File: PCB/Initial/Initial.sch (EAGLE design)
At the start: 19 parts, among them U2 AT24C512C-SHD-B

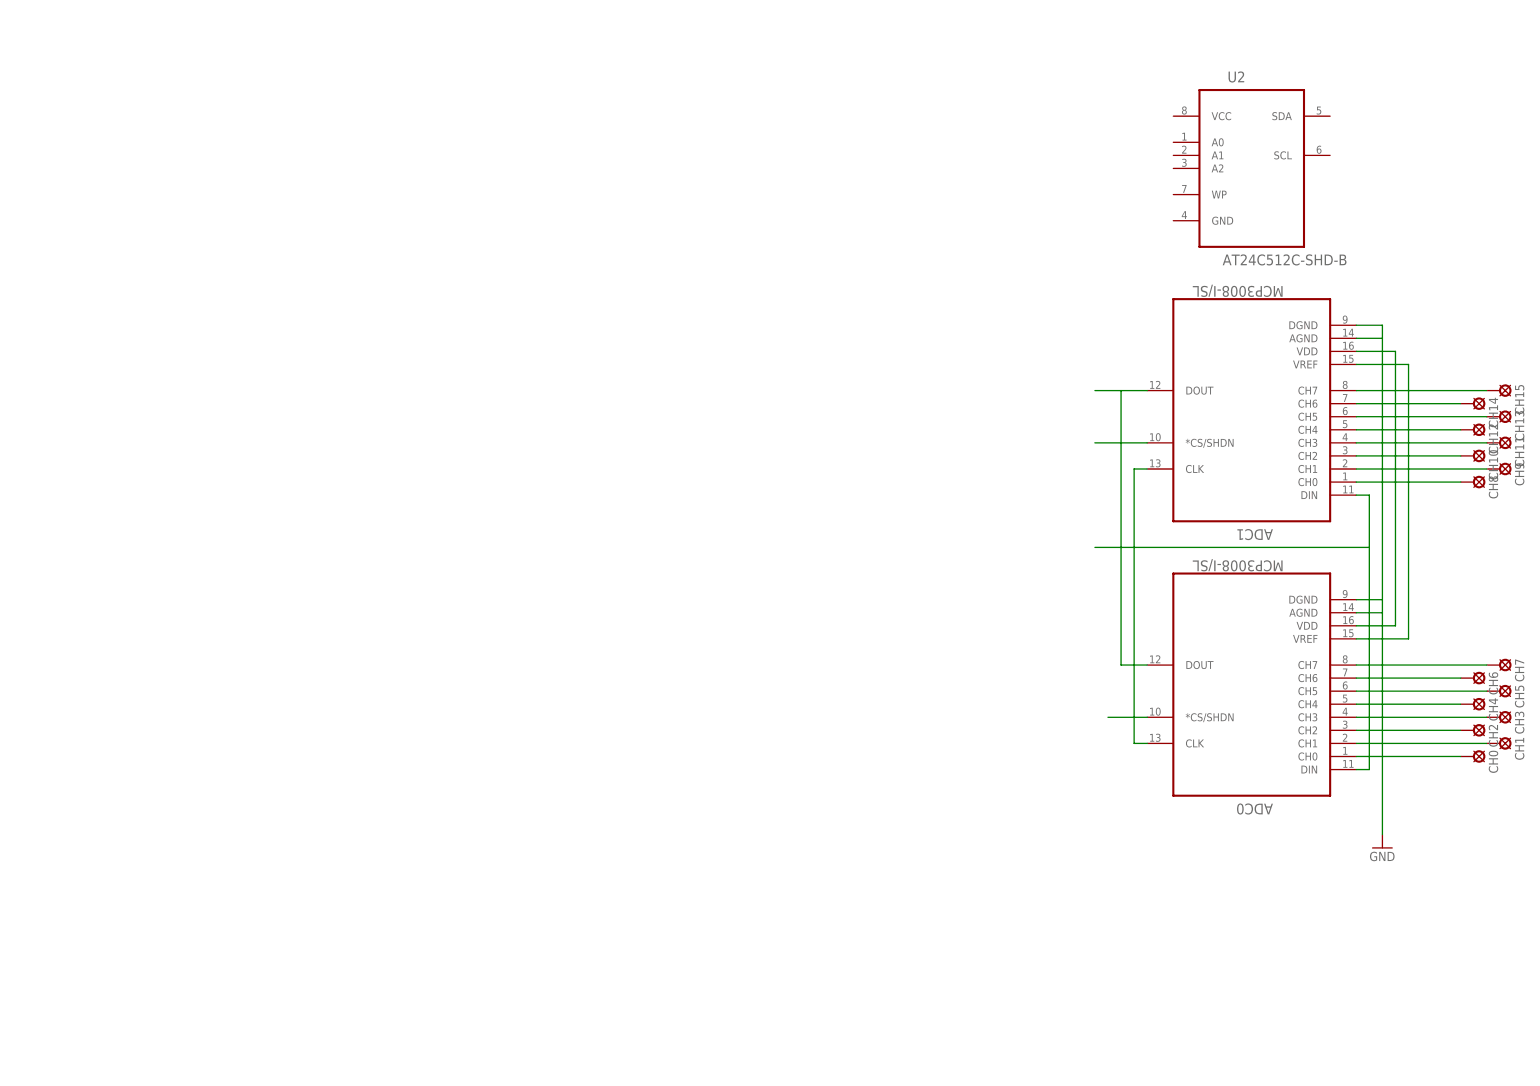
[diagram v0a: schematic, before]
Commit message: Need to draw Xtals, SPI_mini_interface, and probably some more. Might update center of CSR1010A05 with a ground pad. Need to double check SPI compatibility (might be overlayed with I2C)
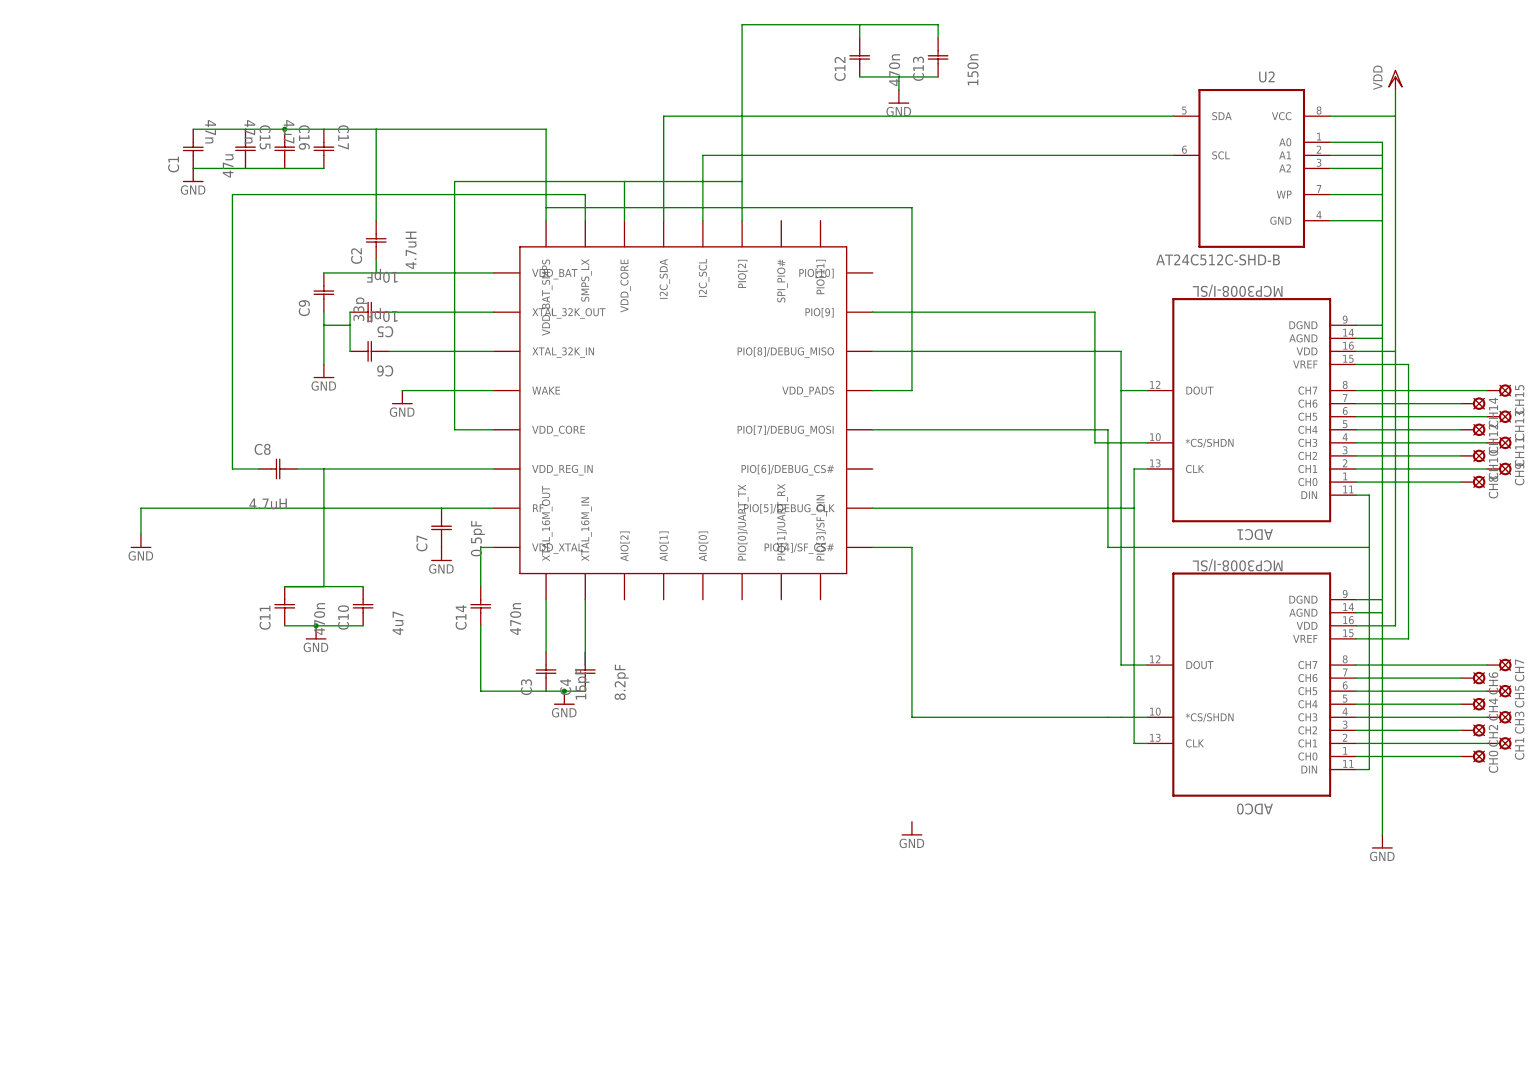
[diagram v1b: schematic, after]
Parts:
- added C1: 47u, AVX_By_element14_Batch_1:UQCL2A100JAT2A/500
- added C10: 4u7, AVX_By_element14_Batch_1:UQCL2A100JAT2A/500
- added C11, C12, C14: 470n, AVX_By_element14_Batch_1:UQCL2A100JAT2A/500
- added C13: 150n, AVX_By_element14_Batch_1:UQCL2A100JAT2A/500
- added C15, C16: 47n, AVX_By_element14_Batch_1:UQCL2A1R0BAT2A/500
- added C17: 4u7, AVX_By_element14_Batch_1:UQCL2A1R0BAT2A/500
- added C2: 4.7uH, AVX_By_element14_Batch_1:UQCL2A100JAT2A/500
- added C3: 15pF, AVX_By_element14_Batch_1:UQCL2A150JAT2A/500
- added C4: 8.2pF, AVX_By_element14_Batch_1:UQCL2A8R2CAT2A/500
- added C5, C6: 10pF, AVX_By_element14_Batch_1:UQCL2A100JAT2A/500
- added C7: 0.5pF, AVX_By_element14_Batch_1:UQCL2A0R5BAT2A/500
- added C8: 4.7uH, AVX_By_element14_Batch_1:1210AC103KAZ1A
- added C9: 33p, AVX_By_element14_Batch_1:UQCL2A100JAT2A/500
- added U$1: CSR1010A05-IQQM-R, CSR1010A05:CSR1010A05-IQQM-R
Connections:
- new net N$17: U$1.I2C_SDA, U2.SDA
- new net N$18: U$1.I2C_SCL, U2.SCL
- new net N$26: C6.C1, U$1.XTAL_32K_IN
- new net N$27: C5.C1, U$1.XTAL_32K_OUT
- new net N$28: C12.C2, C13.C2, U$1.PIO[2], U$1.VDD_CORE, U$1.VDD_CORE@1
- new net N$29: C3.C2, U$1.XTAL_16M_OUT
- new net N$30: U$1.XTAL_16M_IN
- new net N$31: C1.C2, C15.C1, C16.C1, C17.C1, C2.C2, U$1.VDD_BAT_SMPS, U$1.VDD_PADS
- new net N$33: C10.C2, C11.C2, C8.C2, U$1.VDD_REG_IN
- new net N$35: C14.C2, U$1.VDD_XTAL
- new net N$36: C2.C1, C9.C2, U$1.VDD_BAT
- new net VDD: ADC0.VDD, ADC1.VDD, U2.VCC
- net GND: now also C1.C1, C10.C1, C11.C1, C12.C1, C13.C1, C14.C1, C17.C2, C3.C1, C4.C1, C5.C2, C6.C2, C7.C1, C7.C2, C9.C1, U$1.RF, U$1.WAKE, U2.A0, U2.A1, U2.A2, U2.GND, U2.WP
- net N$19: now also C8.C1, U$1.SMPS_LX; no longer ADC0.VDD, ADC1.VDD
- net N$21: now also U$1.PIO[5]/DEBUG_CLK
- net N$22: now also U$1.PIO[8]/DEBUG_MISO
- net N$23: now also U$1.PIO[7]/DEBUG_MOSI
- net N$24: now also U$1.PIO[9]
- net N$25: now also U$1.PIO[4]/SF_CS#

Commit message: need to add xtal footprints, solder bridge components and correct mini 8pin SPI connector
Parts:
- added U$2: 8PIN_SMT_CONNECTOR, MINI_SMT_8_PIN_CONNECTOR:8PIN_SMT_CONNECTOR
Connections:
- removed net N$20: ADC0.VREF, ADC1.VREF
- new net N$31: U$1.PIO[6]/DEBUG_CS#, U$2.SPI_CSB
- net GND: now also C12.C2, C13.C2, C15.C2, C16.C2, U$2.CASE, U$2.CASE@2, U$2.CASE@3, U$2.CASE@4, U$2.GND; no longer C12.C1, C13.C1
- net N$21: now also U$2.SPI_CLK
- net N$22: now also U$2.SPI_MISO; no longer ADC1.DOUT
- net N$23: now also U$2.SPI_MOSI
- net N$28: now also C12.C1, C13.C1; no longer C12.C2, C13.C2, U$1.PIO[2]
- net VDD: now also ADC0.VREF, ADC1.VREF, U$2.VCHG
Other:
- moved on the sheet: C12, C13

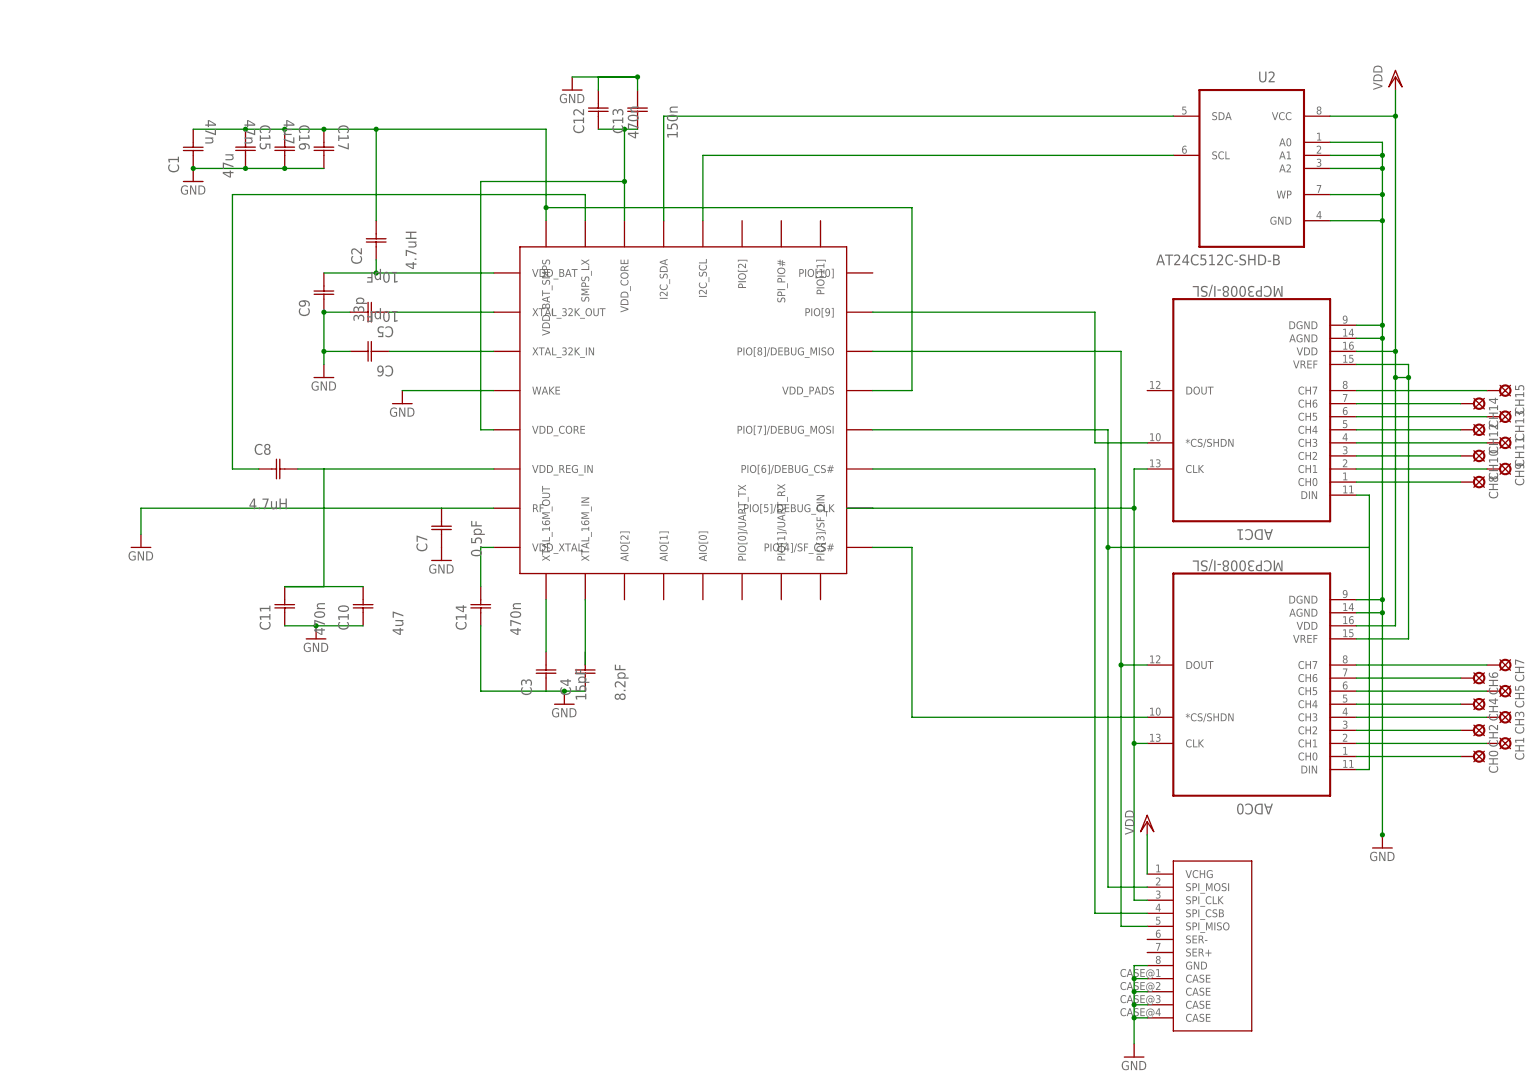
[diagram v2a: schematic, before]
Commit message: xstals done. Connecot and battery need stamping
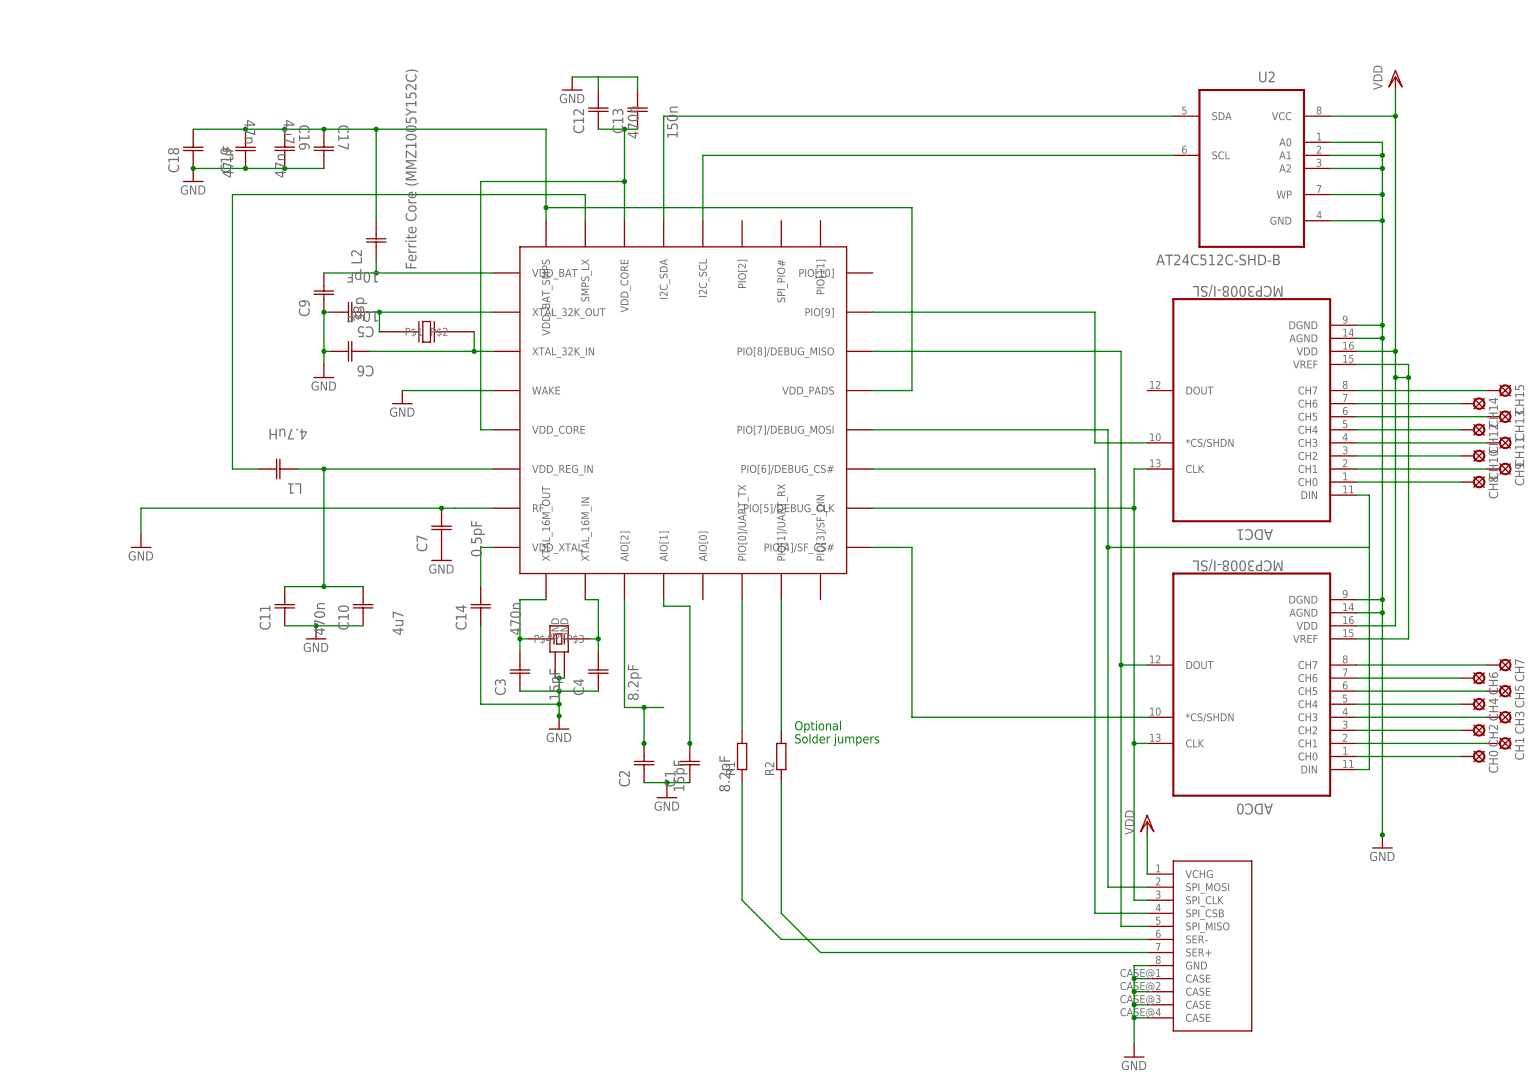
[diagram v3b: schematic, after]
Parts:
- removed C15: 47n, AVX_By_element14_Batch_1:UQCL2A1R0BAT2A/500
- removed C8: 4.7uH, AVX_By_element14_Batch_1:1210AC103KAZ1A
- added C18: 47uF, AVX_By_element14_Batch_1:0805AA100MAT1A
- added C19: 47n, AVX_By_element14_Batch_1:0805AA100MAT1A
- added L1: 4.7uH, AVX_By_element14_Batch_1:12107C102JAT2A
- added L2: Ferrite Core (MMZ1005Y152C), AVX_By_element14_Batch_1:UQCL2A100JAT2A/500
- added R1, R2: (no value), resistor-shunt:BVS
- added U$3: TSX3225, TSX3225:TSX3225
- added U$4: SSP-T7-F, SSP-T7-F:SSP-T7-F
- C1: value 47u -> 8.2pF; device AVX_By_element14_Batch_1:UQCL2A100JAT2A/500 -> AVX_By_element14_Batch_1:UQCL2A8R2CAT2A/500
- C2: value 4.7uH -> 15pF; device AVX_By_element14_Batch_1:UQCL2A100JAT2A/500 -> AVX_By_element14_Batch_1:UQCL2A150JAT2A/500
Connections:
- new net N$20: R1.2, U$2.SER-
- new net N$36: R2.2, U$2.SER+
- new net N$37: R1.1, U$1.PIO[0]/UART_TX
- new net N$38: R2.1, U$1.PIO[1]/UART_RX
- new net N$39: C10.C2, C11.C2, L1.C1, U$1.VDD_REG_IN
- new net N$40: C12.C2
- new net N$41: C2.C2, U$1.AIO[2]
- new net N$42: C1.C1, C2.C1
- net GND: now also C18.C1, C19.C1, U$3.GND@1, U$3.GND@2; no longer C1.C1, C12.C2, C15.C2
- net N$19: now also L1.C2; no longer C8.C1
- net N$27: now also U$4.P$1
- net N$30: now also C4.C2
- net N$32: now also L2.C1; no longer C2.C1
- net N$33: now also C1.C2, U$1.AIO[1]; no longer C10.C2, C11.C2, C8.C2, U$1.VDD_REG_IN
- net N$34: now also C18.C2, C19.C2, L2.C2; no longer C1.C2, C15.C1, C2.C2
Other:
- note added: "Optional"
- note added: "Solder jumpers"
- moved on the sheet: C1, C2, C3, C4, C5, C6
